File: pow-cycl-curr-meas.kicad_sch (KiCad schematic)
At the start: 86 parts, among them Q10 2N7002K-T1-E3, Q6 2N7002K-T1-E3, Q7 2N7002K-T1-E3, Q8 2N7002K-T1-E3, Q9 2N7002K-T1-E3, U10 TCA9534, U11 TMCS1100A2-Q1, U12 TMCS1100A2-Q1, U13 TMCS1100A2-Q1, U14 ADS7828, U8 TMCS1100A2-Q1, U9 TMCS1100A2-Q1

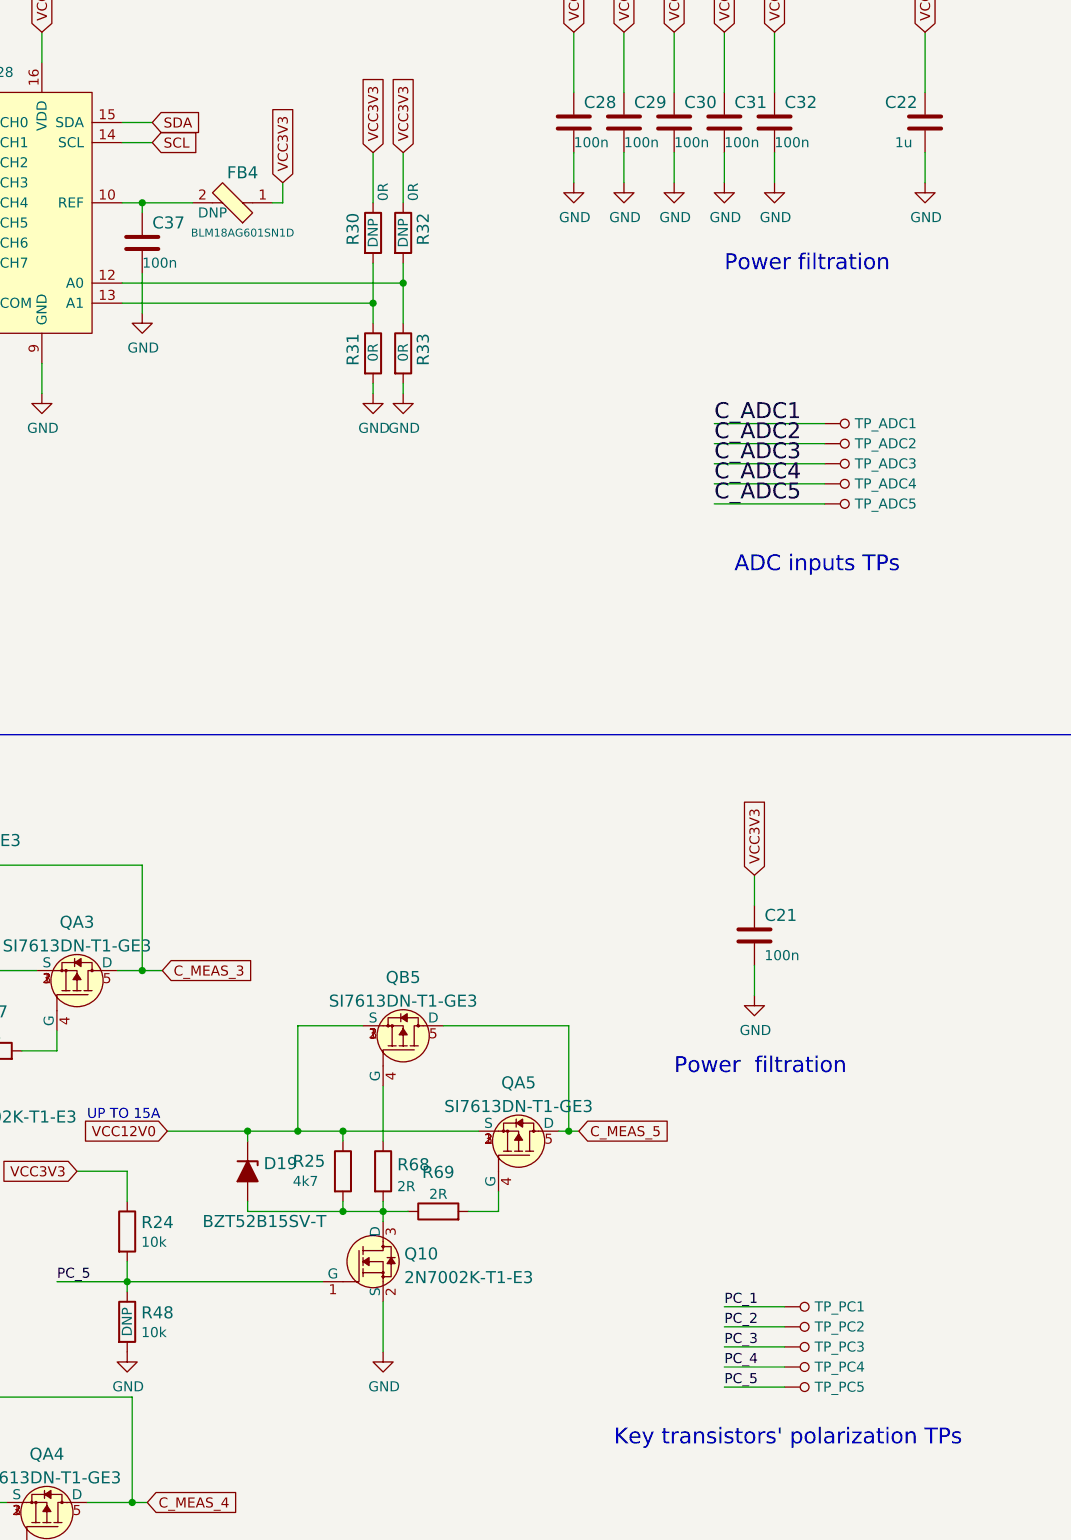
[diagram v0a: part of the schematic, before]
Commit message: Perform globlib and find alterante components
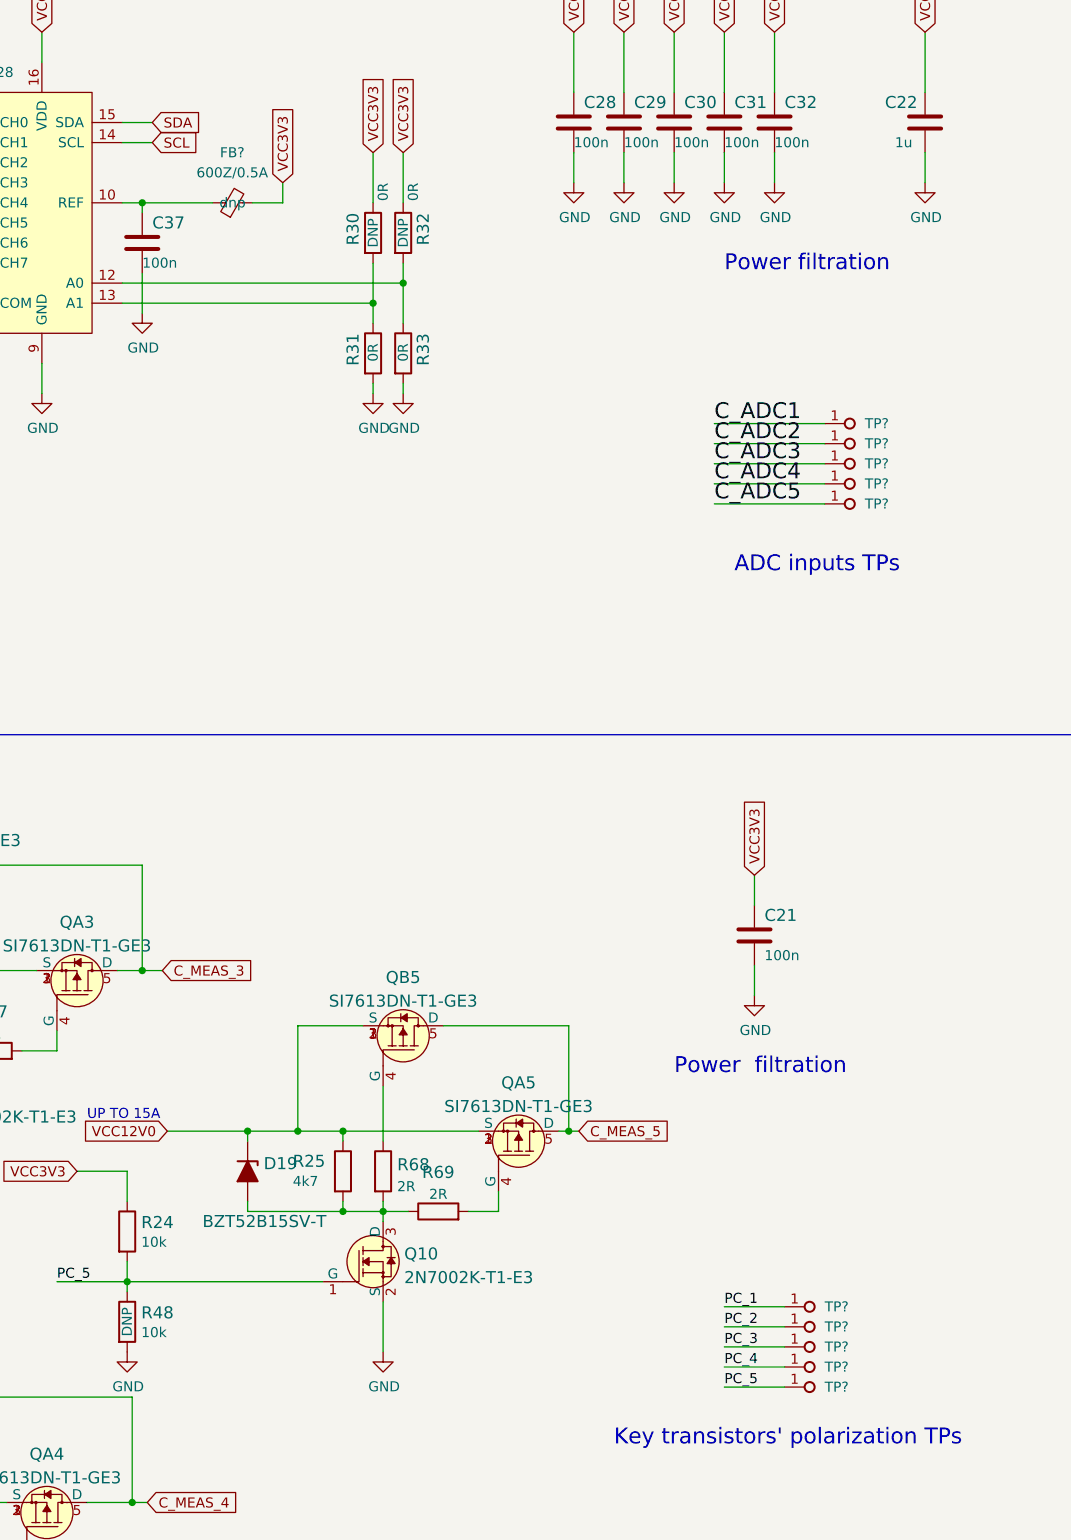
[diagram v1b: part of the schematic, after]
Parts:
- removed FB4: BLM18AG601SN1D, gpu-cluster-backplane-footprints:0603, symbol gpu-cluster-backplane:BLM18AG601SN1D
- removed TP_ADC1, TP_ADC2, TP_ADC3, TP_ADC4, TP_ADC5, TP_PC1, TP_PC2, TP_PC3, TP_PC4, TP_PC5: TP_SMD1MM, gpu-cluster-backplane-footprints:Testpoint_smd_1mm, symbol gpu-cluster-backplane:TP_SMD1MM
- added FB?: FB_600Z_0.5A_Murata-BLM18AG_0603, antmicro-footprints:FB_0603_1608Metric, symbol antmicroFerriteBeadsandChips:FB_600Z_0.5A_Murata-BLM18AG_0603
- added TP? (x10): TP_1mm_SMD, antmicro-footprints:TP_SMD_1mm, symbol antmicroTestPoints:TP_1mm_SMD
- C21, C28, C29, C30, C31, C32, C37: footprint gpu-cluster-backplane-footprints:0402-cap -> antmicro-footprints:C_0402_1005Metric; symbol gpu-cluster-backplane:C_100n_0402 -> antmicroCapacitors0402:C_100n_0402
- C22: footprint gpu-cluster-backplane-footprints:0402-cap -> antmicro-footprints:C_0402_1005Metric; symbol gpu-cluster-backplane:C_1u_0402 -> antmicroCapacitors0402:C_1u_0402
- D20: footprint gpu-cluster-backplane-footprints:TPD2E009DRTR -> antmicro-footprints:TPD2E009DRTR; symbol gpu-cluster-backplane:PESD5V0S2BQA -> antmicroTVSDiodes:PESD5V0S2BQA
- R13, R14, R15, R16, R17, R18, R30, R31, R32, R33, R70: footprint gpu-cluster-backplane-footprints:0402-res -> antmicro-footprints:R_0402_1005Metric; symbol gpu-cluster-backplane:R_0R_0402 -> antmicroResistors0402:R_0R_0402
- R19, R22, R23, R25, R28, R29: footprint gpu-cluster-backplane-footprints:0402-res -> antmicro-footprints:R_0402_1005Metric; symbol gpu-cluster-backplane:R_4k7_0402 -> antmicroResistors0402:R_4k7_0402
- R20, R21, R24, R26, R27, R46, R47, R48, R49, R50: footprint gpu-cluster-backplane-footprints:0402-res -> antmicro-footprints:R_0402_1005Metric; symbol gpu-cluster-backplane:R_10k_0402 -> antmicroResistors0402:R_10k_0402
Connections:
- net C_ADC1: now also TP?.1
- net C_ADC2: now also TP?.1
- net C_ADC3: now also TP?.1
- net C_ADC4: now also TP?.1
- net C_ADC5: now also TP?.1
- net PC_1: now also TP?.1
- net PC_2: now also TP?.1
- net PC_3: now also TP?.1
- net PC_4: now also TP?.1
- net PC_5: now also TP?.1
- net VCC3V3: now also FB?.2
- net at C37.1, U14.10 (REF): now also FB?.1
